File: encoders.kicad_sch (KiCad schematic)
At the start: 110 parts, among them U1 PEL12T-4225S-S1024, U10 WS2811F, U11 WS2811F, U12 WS2811F, U13 WS2811F, U14 WS2811F, U15 WS2811F, U16 WS2811F, U2 PEL12T-4225S-S1024, U3 PEL12T-4225S-S1024, U30 MCP23S17_SS, U31 MCP23S17_SS, U4 PEL12T-4225S-S1024, U5 PEL12T-4225S-S1024, U6 PEL12T-4225S-S1024, U7 PEL12T-4225S-S1024, U8 PEL12T-4225S-S1024, U9 WS2811F

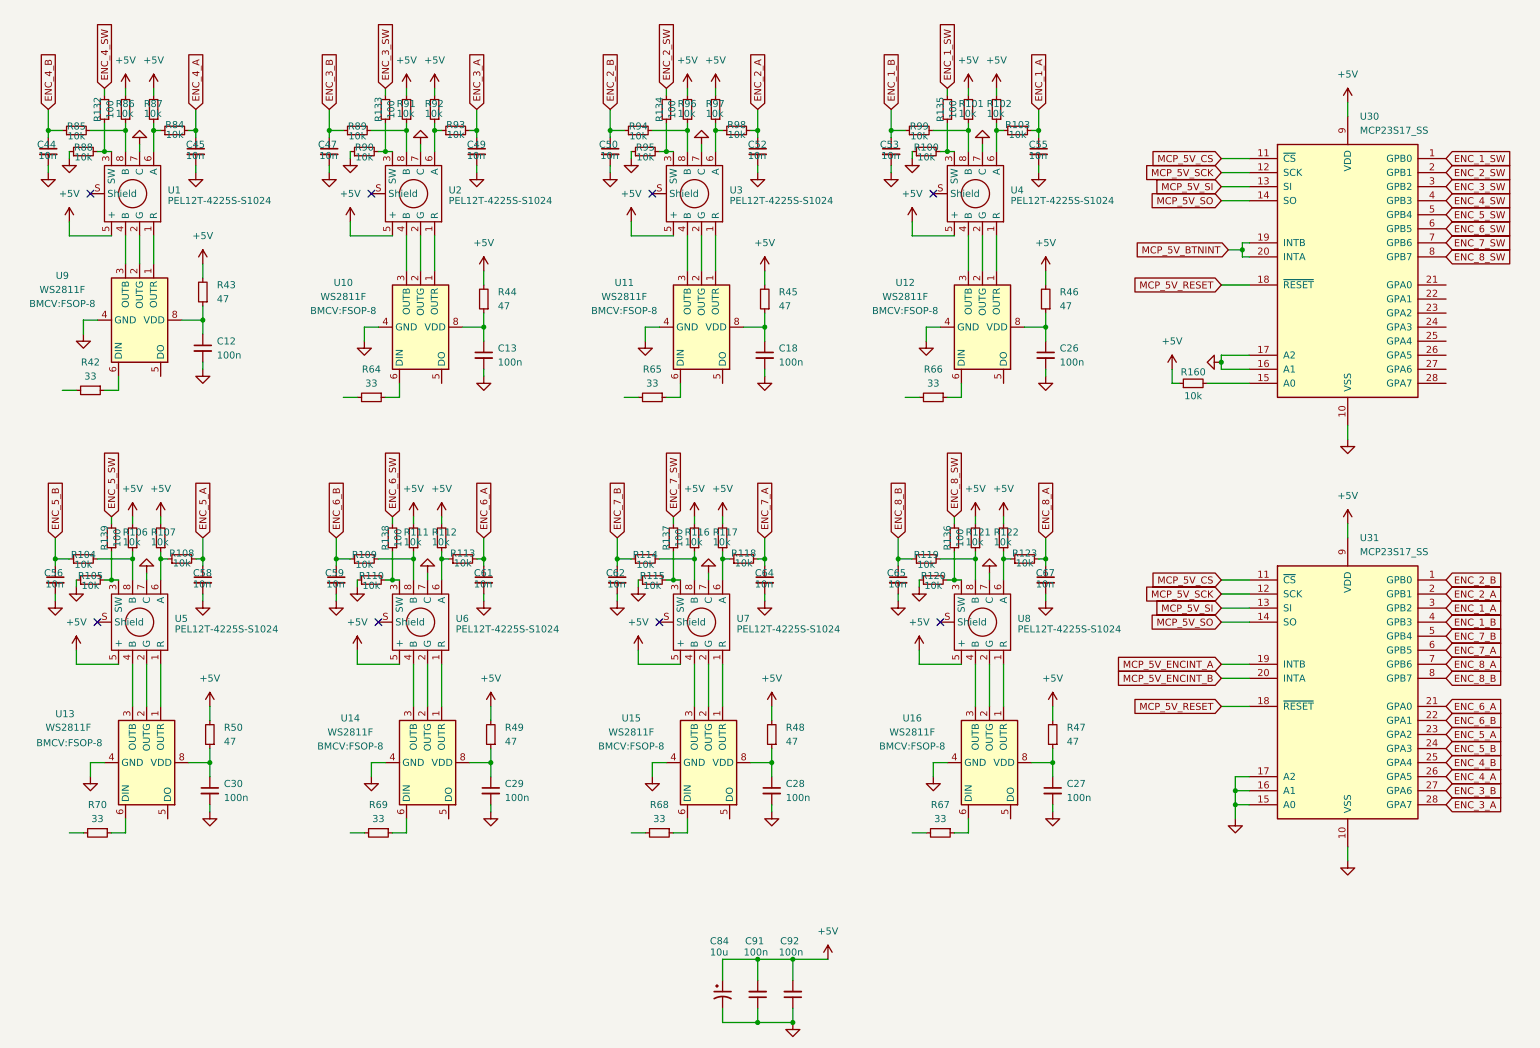
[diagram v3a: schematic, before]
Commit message: switches & led data routing
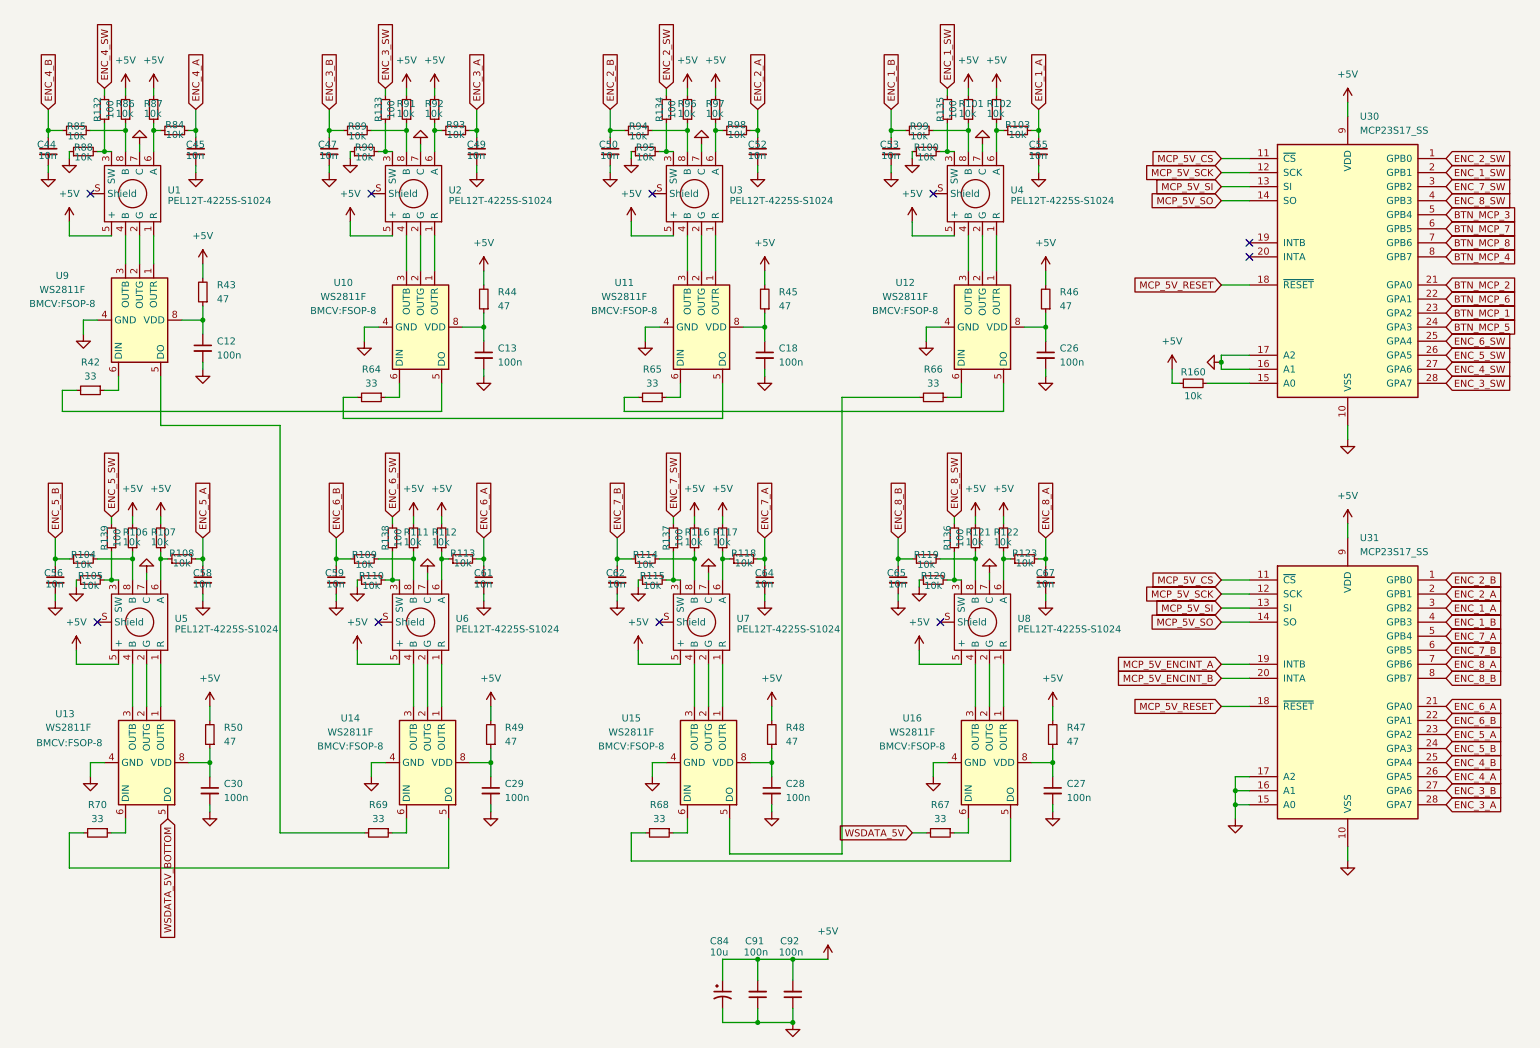
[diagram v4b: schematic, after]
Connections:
- net ENC_1_SW: now also U30.2 (GPB1); no longer U30.1 (GPB0)
- net ENC_2_SW: now also U30.1 (GPB0); no longer U30.2 (GPB1)
- net ENC_3_SW: now also U30.28 (GPA7); no longer U30.3 (GPB2)
- net ENC_4_SW: now also U30.27 (GPA6); no longer U30.4 (GPB3)
- net ENC_5_SW: now also U30.26 (GPA5); no longer U30.5 (GPB4)
- net ENC_6_SW: now also U30.25 (GPA4); no longer U30.6 (GPB5)
- net ENC_7_A: now also U31.5 (GPB4); no longer U31.6 (GPB5)
- net ENC_7_B: now also U31.6 (GPB5); no longer U31.5 (GPB4)
- net ENC_7_SW: now also U30.3 (GPB2); no longer U30.7 (GPB6)
- net ENC_8_SW: now also U30.4 (GPB3); no longer U30.8 (GPB7)
- net at U11.5 (DO): now also R64.2
- net at U10.5 (DO): now also R42.2
- net at U16.5 (DO): now also R68.2
- net BTN_MCP_2: now reaches U30.21 (GPA0)
- net BTN_MCP_6: now reaches U30.22 (GPA1)
- net BTN_MCP_1: now reaches U30.23 (GPA2)
- net BTN_MCP_5: now reaches U30.24 (GPA3)
- net at R66.2: now also U15.5 (DO)
- net at U14.5 (DO): now also R70.2
- net at R69.2: now also U9.5 (DO)
- net WSDATA_5V: now reaches R67.2
- net at R65.2: now also U12.5 (DO)
- net WSDATA_5V_BOTTOM: now reaches U13.5 (DO)
- net MCP_5V_BTNINT: no longer names the net of U30.19 (INTB)
- net MCP_5V_BTNINT: no longer U30.20 (INTA)
- new net BTN_MCP_3: U30.5 (GPB4)
- new net BTN_MCP_4: U30.8 (GPB7)
- new net BTN_MCP_7: U30.6 (GPB5)
- new net BTN_MCP_8: U30.7 (GPB6)
- no-connect marks 8 -> 10

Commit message: alpha
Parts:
- removed C84: 10u, Capacitor_Tantalum_SMD:CP_EIA-3216-18_Kemet-A, symbol Device:C_Polarized_Small_US
- added C84: 10u, Capacitor_SMD:C_0805_2012Metric, symbol Device:C_Small
- C12, C13, C18, C26, C27, C28, C29, C30: LCSC Part # (none) -> C307331
- C44, C45, C47, C49, C50, C52, C53, C55, C56, C58, C59, C61, C62, C64, C65, C67: LCSC Part # (none) -> C15195
- C91, C92: LCSC Part # (none) -> C14663
- R100, R101, R102, R103, R104, R105, R106, R107, R108, R109, R110, R111, R112, R113, R114, R115, R116, R117, R118, R119, R120, R121, R122, R123, R160, R84, R85, R86, R87, R88, R89, R90, R91, R92, R93, R94, R95, R96, R97, R98, R99: LCSC Part # (none) -> C25744
- R132, R133, R134, R135, R136, R137, R138, R139: LCSC Part # (none) -> C25076
- R42, R64, R65, R66, R67, R68, R69, R70: LCSC Part # (none) -> C25105
- R43, R44, R45, R46, R47, R48, R49, R50: value 47 -> 100; LCSC Part # (none) -> C25076
- U1, U2, U3, U4, U5, U6, U7, U8: now not fitted
- U10, U11, U12, U13, U14, U15, U16, U9: LCSC Part # (none) -> C5446692
- U30, U31: LCSC Part # (none) -> C128577
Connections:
- net +5V: now also C84.2
- net GND: now also C84.1

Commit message: update
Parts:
- U1, U2, U3, U4, U5, U6, U7, U8: now fitted
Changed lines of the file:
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@@
 		(in_bom yes)
 		(on_board yes)
-		(dnp yes)
+		(dnp no)
 		(fields_autoplaced yes)
 		(property "Reference" "U5"
@@
 		(in_bom yes)
 		(on_board yes)
-		(dnp yes)
+		(dnp no)
 		(fields_autoplaced yes)
 		(property "Reference" "U8"
@@
 		(in_bom yes)
 		(on_board yes)
-		(dnp yes)
+		(dnp no)
 		(fields_autoplaced yes)
 		(property "Reference" "U4"
@@
 		(in_bom yes)
 		(on_board yes)
-		(dnp yes)
+		(dnp no)
 		(fields_autoplaced yes)
 		(property "Reference" "U7"
@@
 		(in_bom yes)
 		(on_board yes)
-		(dnp yes)
+		(dnp no)
 		(fields_autoplaced yes)
 		(property "Reference" "U6"
@@
 		(in_bom yes)
 		(on_board yes)
-		(dnp yes)
+		(dnp no)
 		(property "Reference" "U2"
 			(at 95.25 37.4649 0)
@@
 		(in_bom yes)
 		(on_board yes)
-		(dnp yes)
+		(dnp no)
 		(fields_autoplaced yes)
 		(property "Reference" "U3"
@@
 		(in_bom yes)
 		(on_board yes)
-		(dnp yes)
+		(dnp no)
 		(property "Reference" "U1"
 			(at 44.45 37.4649 0)

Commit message: first ordered verrsion
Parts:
- removed R160: 10k, Resistor_SMD:R_0402_1005Metric, symbol Device:R_Small
- R43, R44, R45, R46, R47, R48, R49, R50: value 100 -> 10; LCSC Part # C25076 -> C25077
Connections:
- net +5V: now also U30.15 (A0)
